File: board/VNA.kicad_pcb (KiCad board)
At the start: 2 copper layers, 100 x 100 mm, 140 parts, among them J1 Conn_01x08, J10 Conn_01x01, J11 Conn_01x01, J12 Conn_01x01, J13 Conn_01x01, J14 Conn_01x01, J15 Conn_02x05_Odd_Even, J16 Conn_02x05_Odd_Even, J17 Conn_01x04, J18 Conn_01x01, J19 Conn_01x01, J2 Conn_Coaxial, J20 Conn_01x01, J21 Conn_01x01, J22 Conn_01x02, J3 Conn_01x01, J4 Conn_01x01, J5 Conn_01x01, J6 Conn_01x01, J7 Conn_01x01, J9 Conn_Coaxial, U1 SI5351A, U2 74HC14, U3 SA612, U4 SA612, U5 SA612, U6 TL082, U7 TL082, U8 SA612, U9 LM7805_TO220, Y1 27 MHz

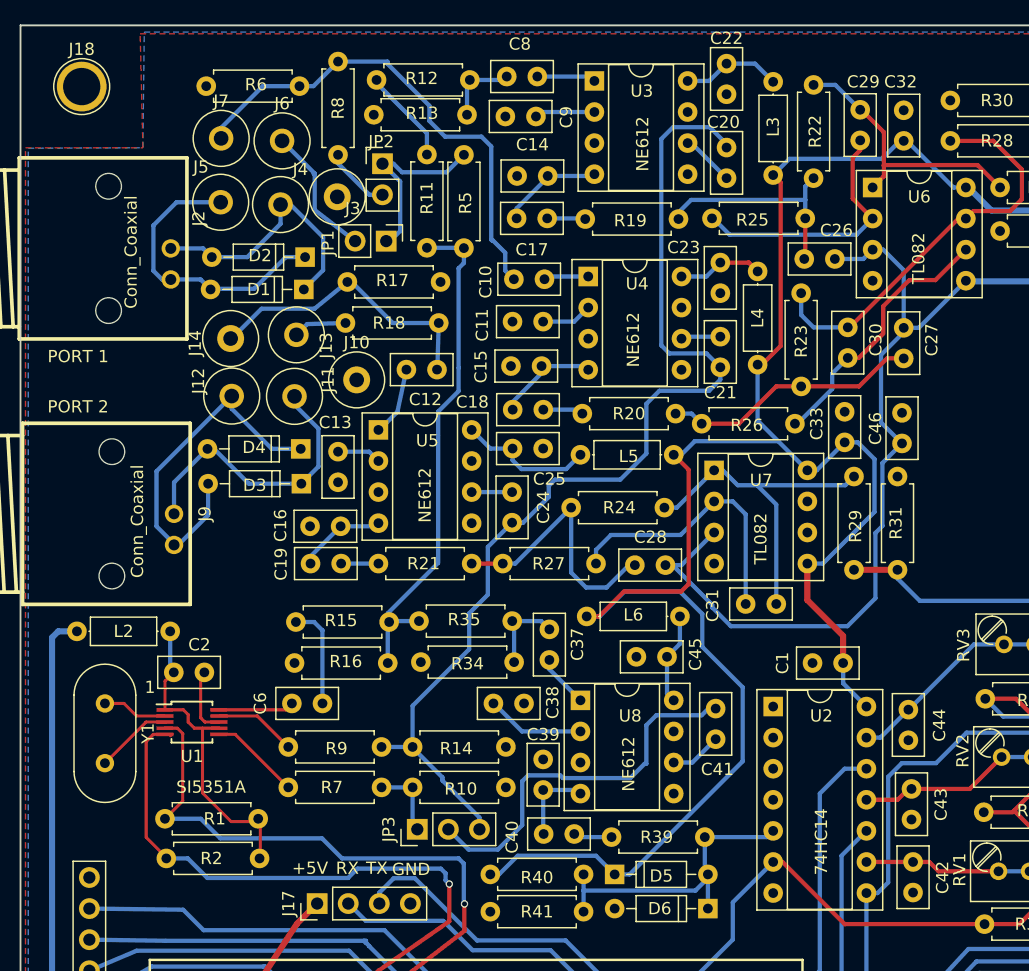
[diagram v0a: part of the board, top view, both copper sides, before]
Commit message: Made continuous ground plane over most of the part
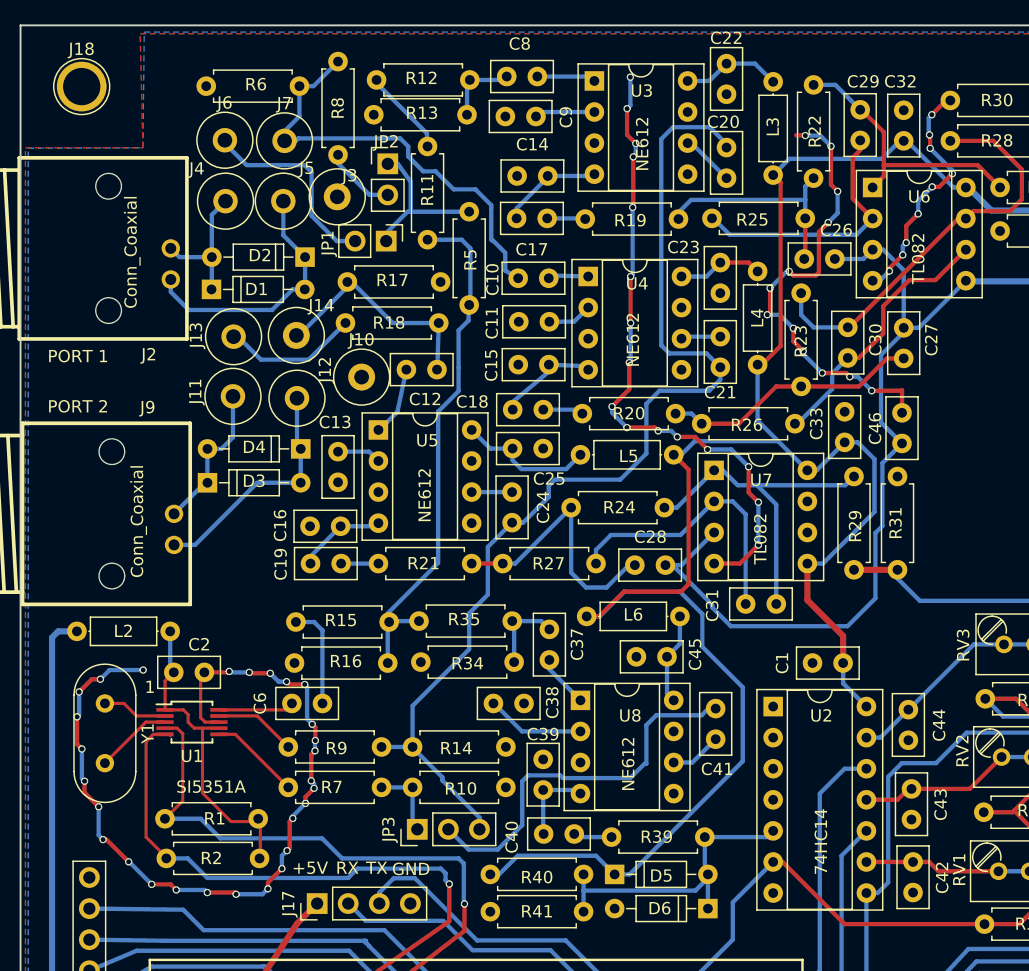
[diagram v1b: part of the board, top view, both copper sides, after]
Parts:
- moved D3 7.67 mm to (65.3, 87.4), turned to 0 degrees
- moved D1 7.54 mm to (65.6, 71.6), turned to 0 degrees
- moved J14 5.38 mm to (72.5, 75.3)
- moved J12 5.34 mm to (72.6, 80.5)
- moved J7 5.19 mm to (71.6, 59.4)
- moved J13 5.13 mm to (67.4, 75.4)
- moved J5 5.12 mm to (71.5, 64.4)
- moved J11 5.03 mm to (67.4, 80.3)
- moved J6 4.67 mm to (66.7, 59.4)
- moved R5 4.67 mm to (86.7, 65.2)
- moved J4 4.50 mm to (66.8, 64.4)
- moved R11 0.66 mm to (83.3, 59.9)
- moved C15 0.61 mm to (90.7, 77.7)
- moved C11 0.51 mm to (93.2, 74.2)
- moved J10 0.47 mm to (77.9, 78.7)
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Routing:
- net GND: track 5.47 -> 177.6 mm, vias 0 -> 65
- net Net-(D3-Pad1): track 24.7 -> 12.9 mm
- net Net-(D1-Pad1): track 21.6 -> 11.3 mm
- net Net-(D3-Pad2): track 29.8 -> 19.9 mm
- net Net-(J13-Pad1): track 4.38 -> 11.3 mm
- net Net-(J6-Pad1): track 11.1 -> 16.3 mm
- net SAMPCUR2: track 24.2 -> 19.1 mm
- net SAMPCUR: track 40.7 -> 35.9 mm
- net Net-(D1-Pad2): track 24.3 -> 21.2 mm
- net CLK0: track 42.3 -> 43.9 mm
- net Net-(JP1-Pad1): track 15.3 -> 13.8 mm
- net Net-(R11-Pad1): track 7.80 -> 7.14 mm
- net Net-(C11-Pad1): track 4.16 -> 3.65 mm

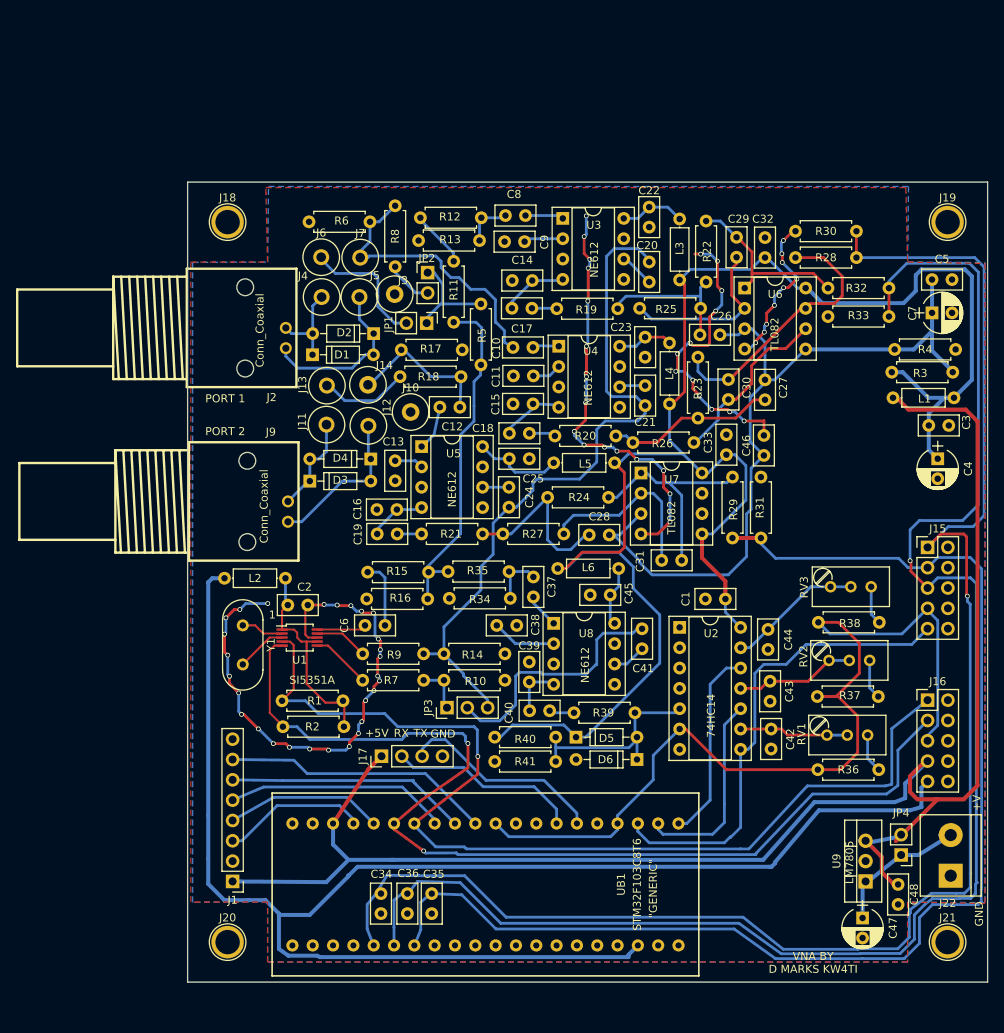
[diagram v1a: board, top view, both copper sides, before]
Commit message: Removed useless parts of the board and make some corrections
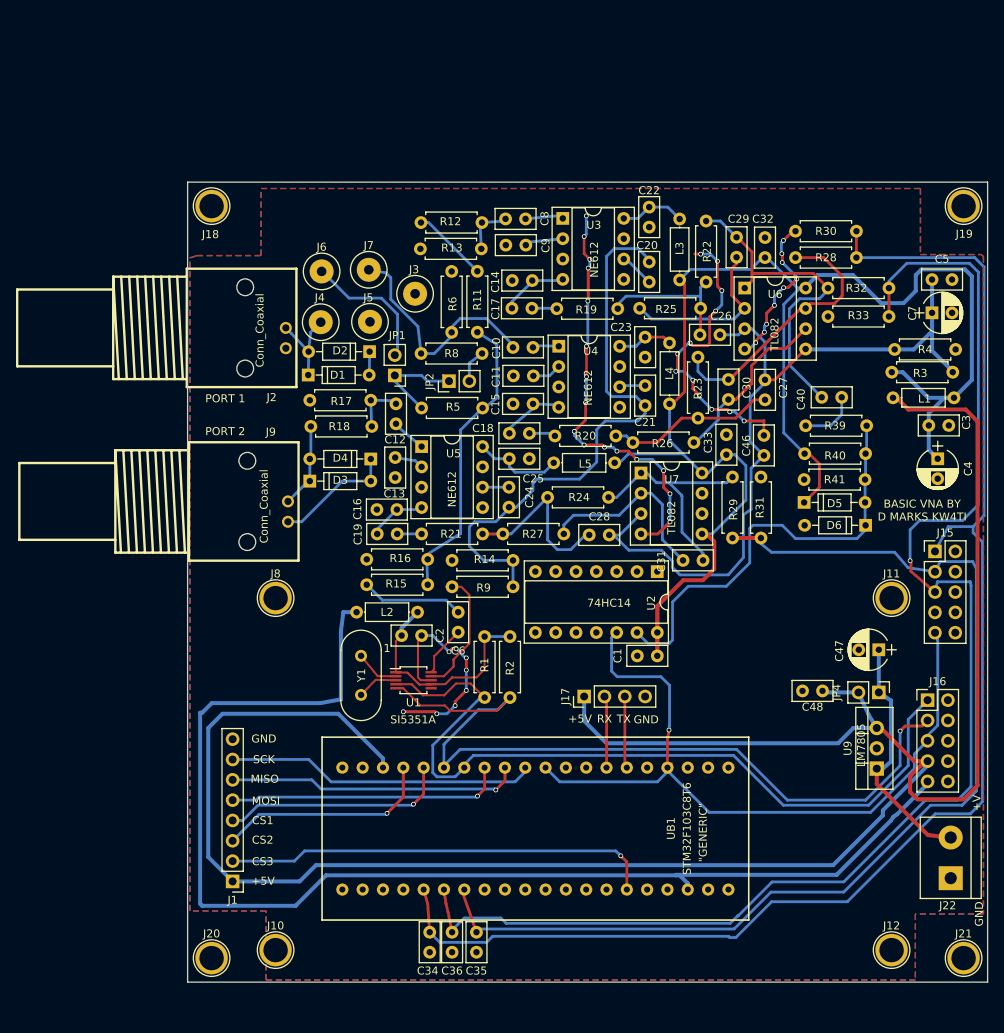
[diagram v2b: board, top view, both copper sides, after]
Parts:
- removed C37, C38, C41, C42: 10 nF, Capacitors_THT:C_Disc_D5.0mm_W2.5mm_P2.50mm
- removed C39: 330 pF, Capacitors_THT:C_Disc_D5.0mm_W2.5mm_P2.50mm
- removed C43, C45: 100 nF, Capacitors_THT:C_Disc_D5.0mm_W2.5mm_P2.50mm
- removed C44: 1 nF, Capacitors_THT:C_Disc_D5.0mm_W2.5mm_P2.50mm
- removed J13, J14: Conn_01x01, Connectors:1pin
- removed JP3: Jumper_NC_Dual, Pin_Headers:Pin_Header_Straight_1x03_Pitch2.54mm
- removed L6: Ferrite_Bead_Small, Inductors_THT:L_Axial_L5.3mm_D2.2mm_P7.62mm_Horizontal_Vishay_IM-1
- removed R10, R34: 51R, Resistors_THT:R_Axial_DIN0207_L6.3mm_D2.5mm_P7.62mm_Horizontal
- removed R35, R7: 1.5k, Resistors_THT:R_Axial_DIN0207_L6.3mm_D2.5mm_P7.62mm_Horizontal
- removed R36, R37, R38: 2.2k, Resistors_THT:R_Axial_DIN0207_L6.3mm_D2.5mm_P7.62mm_Horizontal
- removed RV1, RV2, RV3: 22k, Potentiometers:Potentiometer_Trimmer_Bourns_3296W
- removed U8: SA612, Housings_DIP:DIP-8_W7.62mm_Socket
- added J8: Conn_01x01, Connectors:1pin, F.Cu at (61.0, 102.0)
- C10, C11, C12, C13, C20, C21, C24, C6, C8, C9: value 10 nF -> 100 nF
- R15: value 510R -> 0R
- R17: value 5R1 -> 4R7
- R18: value 51R -> 47R
- R19, R20, R21, R25, R26, R27: value 10k -> 1k5
- R22, R23, R24: value 47k -> 68k
- moved J12 92.6 mm to (138.0, 146.0)
- moved J11 73.9 mm to (138.0, 102.0)
- moved J10 69.3 mm to (61.0, 146.0)
- moved C40 53.6 mm to (131.8, 76.9)
- moved R40 52.5 mm to (134.7, 83.9)
- moved R41 52.3 mm to (127.1, 87.2)
- moved R39 46.1 mm to (134.9, 80.5)
- moved D5 40.9 mm to (127.1, 90.0)
- moved D6 40.9 mm to (134.7, 92.9)
- moved C47 33.6 mm to (136.4, 108.5), turned to 180 degrees
- moved R2 28.6 mm to (90.3, 114.4), turned to 90 degrees
- moved J17 26.4 mm to (99.6, 114.3)
- moved C48 26.0 mm to (129.4, 113.6), turned to 180 degrees
- moved R1 25.3 mm to (87.1, 114.4), turned to 90 degrees
- moved JP4 20.5 mm to (136.4, 113.8), turned to 270 degrees
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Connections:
- C40 pad 2: Net-(C39-Pad2) -> Net-(C29-Pad1)
- D1 pad 2: Net-(D1-Pad2) -> GND
- D2 pad 1: Net-(D1-Pad2) -> GND
- D3 pad 2: Net-(D3-Pad2) -> GND
- D4 pad 1: Net-(D3-Pad2) -> GND
- J1 pad 2: (no net) -> PB10
- J10 pad 1: GND -> (no net)
- J11 pad 1: Net-(D3-Pad1) -> (no net)
- J12 pad 1: Net-(D3-Pad2) -> (no net)
- J15 pad 7: SYNCSAMPLE -> (no net)
- J15 pad 9: SYNCSAMPLEP1 -> SYNCSAMPLE
- J2 pad 2: Net-(D1-Pad2) -> GND
- J5 pad 1: Net-(D1-Pad2) -> GND
- J9 pad 2: Net-(D3-Pad2) -> GND
- R18 pad 2: Net-(J13-Pad1) -> Net-(D3-Pad1)
- U1 pad 6: Net-(R7-Pad2) -> (no net)
- U2 pad 10: SYNCSAMPLEP2 -> (no net)
- U2 pad 11: Net-(C43-Pad1) -> GND
- U2 pad 12: SYNCSAMPLEP3 -> SYNCSAMPLE
- U2 pad 13: Net-(C44-Pad1) -> Net-(D5-Pad2)
- U2 pad 5: Net-(D5-Pad2) -> GND
- U2 pad 6: SYNCSAMPLE -> (no net)
- U2 pad 8: SYNCSAMPLEP1 -> (no net)
- U2 pad 9: Net-(C42-Pad1) -> GND
- U9 pad 2: (no net) -> GND
- UB1 pad 21: (no net) -> PB10
- UB1 pad 25: SYNCSAMPLEP3 -> (no net)
- UB1 pad 26: SYNCSAMPLEP2 -> (no net)
- UB1 pad 27: SYNCSAMPLEP1 -> (no net)
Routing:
- net +5V: track 204.1 -> 271.6 mm
- net SYNCSAMPLEP1: track 60.3 -> 0.00 mm
- net PB10: track 0.00 -> 53.8 mm, vias 0 -> 1
- net +3V3: track 190.5 -> 154.9 mm
- net Net-(C41-Pad2): track 31.4 -> 0.00 mm
- net SDA: track 130.9 -> 100.5 mm, vias 2 -> 1
- net FILT5V: track 218.1 -> 188.4 mm
- net Net-(D5-Pad2): track 25.7 -> 54.9 mm
- net SCL: track 128.2 -> 100.2 mm, vias 1 -> 0
- net SYNCSAMPLEP2: track 25.1 -> 0.00 mm
- net SYNCSAMPLEP3: track 24.3 -> 0.00 mm
- net DEMODCUR: track 200.4 -> 176.7 mm, vias 1 -> 0
- net DEMODVOLT: track 197.5 -> 174.7 mm
- net DEMODCUR2: track 159.6 -> 137.5 mm
- net Net-(D1-Pad2): track 21.2 -> 0.00 mm
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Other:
- board text added: "BASIC VNA BY D MARKS KW4TI"
- board text added: "CS1"
- board text added: "CS2"
- board text added: "CS3"
- board text added: "MISO"
- board text added: "MOSI"
- board text added: "SCK"
- board text removed: "VNA BY D MARKS KW4TI"

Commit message: Added LCD mount
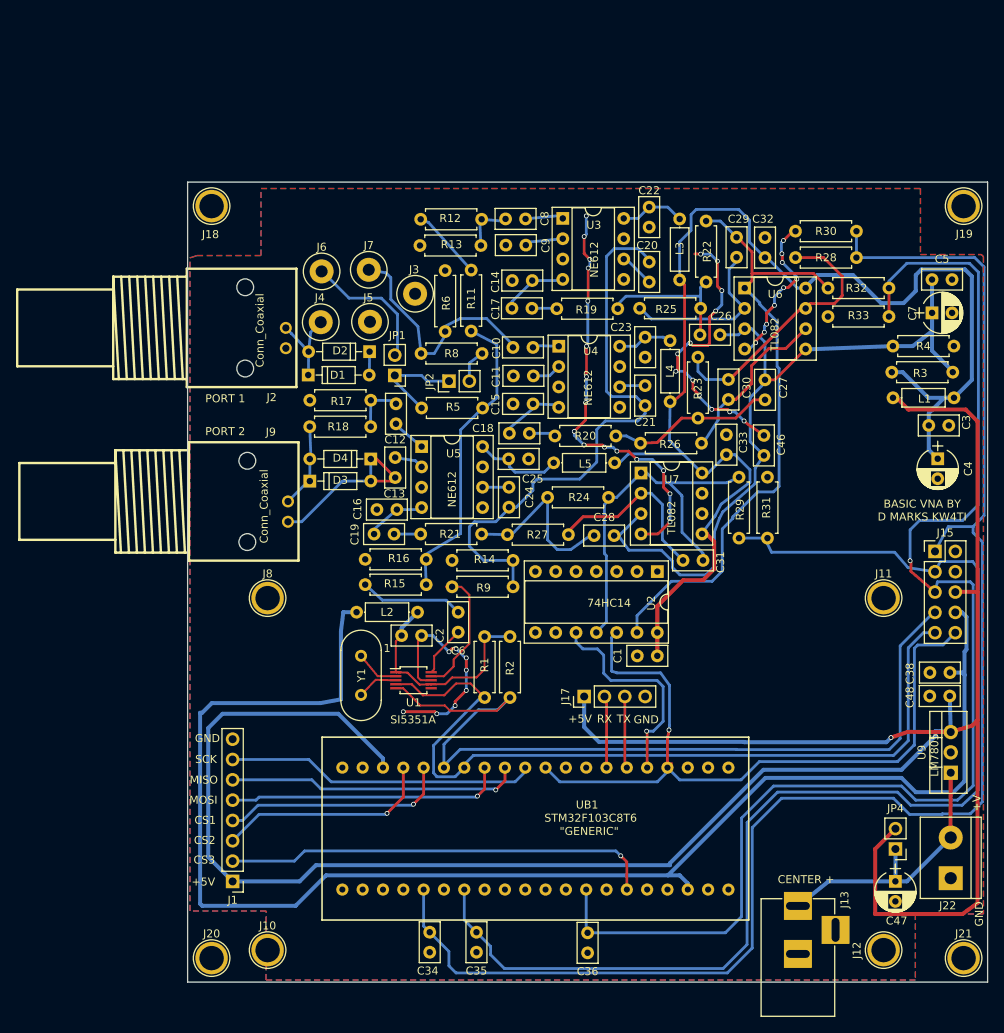
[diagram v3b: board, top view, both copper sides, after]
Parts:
- removed C40: 100 nF, Capacitors_THT:C_Disc_D5.0mm_W2.5mm_P2.50mm
- removed D5, D6: 1N4148, Diodes_THT:D_DO-35_SOD27_P7.62mm_Horizontal
- removed J16: Conn_02x05_Odd_Even, Pin_Headers:Pin_Header_Straight_2x05_Pitch2.54mm
- removed R39: 1k, Resistors_THT:R_Axial_DIN0207_L6.3mm_D2.5mm_P7.62mm_Horizontal
- removed R40, R41: 10k, Resistors_THT:R_Axial_DIN0207_L6.3mm_D2.5mm_P7.62mm_Horizontal
- added C38: 100 nF, Capacitors_THT:C_Disc_D5.0mm_W2.5mm_P2.50mm, F.Cu at (145.3, 111.3)
- added J13: Barrel_Jack, Connectors:BARREL_JACK, F.Cu at (126.3, 140.5)
- R3, R4: value 1k -> 470R
- moved C47 29.0 mm to (138.5, 137.4), turned to 270 degrees
- moved JP4 19.7 mm to (138.5, 133.4), turned to 180 degrees
- moved C36 16.9 mm to (100.0, 143.8)
- moved C48 15.9 mm to (145.3, 114.2)
- moved U9 9.26 mm to (145.4, 123.8)
- moved J10 1.00 mm to (60.0, 146.0)
- moved J11 1.00 mm to (137.0, 102.0)
- moved J12 1.00 mm to (137.0, 146.0)
- moved J8 1.00 mm to (60.0, 102.0)
- moved R26 0.96 mm to (114.2, 82.6)
- moved R6 0.82 mm to (82.2, 68.7)
- moved R31 0.81 mm to (122.5, 86.9)
- moved R29 0.81 mm to (118.9, 94.5)
- moved R11 0.79 mm to (85.4, 61.0)
- moved C28 0.61 mm to (100.8, 94.2)
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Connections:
- J15 pad 10: GND -> SYNCSAMPLE
- J15 pad 6: GND -> +5V
- J15 pad 7: (no net) -> SDA
- J15 pad 8: GND -> +3V3
- J15 pad 9: SYNCSAMPLE -> SCL
- U2 pad 10: (no net) -> SYNCSAMPLE2
- U2 pad 11: GND -> Net-(C31-Pad1)
- U2 pad 13: Net-(D5-Pad2) -> Net-(C29-Pad1)
- UB1 pad 11: DEMODVOLT -> (no net)
- UB1 pad 18: (no net) -> DEMODVOLT
- UB1 pad 29: (no net) -> SYNCSAMPLE2
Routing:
- net Net-(D5-Pad2): track 54.9 -> 0.00 mm
- net Net-(C29-Pad1): track 41.6 -> 79.4 mm
- net +5V: track 271.6 -> 303.7 mm, vias 0 -> 1
- net +3V3: track 154.9 -> 186.1 mm
- net SYNCSAMPLE2: track 0.00 -> 27.2 mm, vias 0 -> 1
- net FILT5V: track 188.4 -> 168.4 mm
- net Net-(C31-Pad1): track 29.0 -> 47.6 mm
- net DEMODCUR2: track 137.5 -> 153.0 mm
- net DEMODCUR: track 176.7 -> 191.6 mm
- net DEMODVOLT: track 174.7 -> 166.3 mm
- net Net-(C40-Pad1): track 7.25 -> 0.00 mm
- net GND: track 157.1 -> 163.1 mm
- net SDA: track 100.5 -> 106.1 mm, vias 1 -> 0
- net SCL: track 100.2 -> 102.8 mm
- net Net-(C47-Pad1): track 32.4 -> 35.0 mm
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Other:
- board text added: "CENTER +"
